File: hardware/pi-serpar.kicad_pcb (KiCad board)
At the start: 2 copper layers, 65 x 56 mm, 31 parts, among them J2 40HAT, J3 IEEE1284, J4 IEEE1284, J5 RS232, J7 RS232, U1 CAT24C32, U2 SN74LVC161284DLR, U3 MAX3232

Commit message: v1 ordered at jlcpcb
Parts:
- JP1: footprint Jumper:SolderJumper-2_P1.3mm_Open_RoundedPad1.0x1.5mm -> Jumper:SolderJumper-2_P1.3mm_Bridged_Pad1.0x1.5mm
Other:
- board text added: "2"
- board text added: "3"
- board text added: "7"
- board text added: "8"
- board text added: "DB9 Pins"
- board text added: "RS232 setup"
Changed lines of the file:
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@@
       ))
   )
-  (footprint "Jumper:SolderJumper-2_P1.3mm_Open_RoundedPad1.0x1.5mm" (layer "B.Cu")
+  (footprint "Jumper:SolderJumper-2_P1.3mm_Bridged_Pad1.0x1.5mm" (layer "B.Cu")
     (at 135.748 71.882)
-    (descr "SMD Solder Jumper, 1x1.5mm, rounded Pads, 0.3mm gap, open")
-    (tags "solder jumper open")
+    (descr "SMD Solder Jumper, 1x1.5mm Pads, 0.3mm gap, bridged with 1 copper strip")
+    (tags "net tie solder jumper bridged")
     (property "Sheetfile" "pi-serpar.kicad_sch")
     (property "Sheetname" "")
-    (property "ki_description" "Solder Jumper, 2-pole, open")
+    (property "ki_description" "Solder Jumper, 2-pole, closed/bridged")
     (property "ki_keywords" "solder jumper SPST")
     (attr exclude_from_pos_files)
-    (fp_text reference "JP1" (at 0 1.8) (layer "B.SilkS") hide
+    (net_tie_pad_groups "1, 2")
+    (fp_text reference "JP1" (at 0 1.8 180) (layer "B.SilkS")
         (effects (font (size 1 1) (thickness 0.15)) (justify mirror))
     )
-    (fp_text value "EEPROM WP" (at 0 -1.9) (layer "B.SilkS")
+    (fp_text value "EEPROM WP" (at 0 -1.9 180) (layer "B.Fab")
         (effects (font (size 1 1) (thickness 0.15)) (justify mirror))
     )
-    (fp_line (start -1.4 -0.3) (end -1.4 0.3)
-      (stroke (width 0.12) (type solid)) (layer "B.SilkS"))
-    (fp_line (start -0.7 1) (end 0.7 1)
-      (stroke (width 0.12) (type solid)) (layer "B.SilkS"))
-    (fp_line (start 0.7 -1) (end -0.7 -1)
-      (stroke (width 0.12) (type solid)) (layer "B.SilkS"))
-    (fp_line (start 1.4 0.3) (end 1.4 -0.3)
-      (stroke (width 0.12) (type solid)) (layer "B.SilkS"))
-    (fp_arc (start -1.4 -0.3) (mid -1.194975 -0.794975) (end -0.7 -1)
-      (stroke (width 0.12) (type solid)) (layer "B.SilkS"))
-    (fp_arc (start -0.7 1) (mid -1.194975 0.794975) (end -1.4 0.3)
-      (stroke (width 0.12) (type solid)) (layer "B.SilkS"))
-    (fp_arc (start 0.7 -1) (mid 1.194975 -0.794975) (end 1.4 -0.3)
-      (stroke (width 0.12) (type solid)) (layer "B.SilkS"))
-    (fp_arc (start 1.4 0.3) (mid 1.194975 0.794975) (end 0.7 1)
+    (fp_poly
+      (pts
+        (xy -0.25 0.3)
+        (xy 0.25 0.3)
+        (xy 0.25 -0.3)
+        (xy -0.25 -0.3)
+      )
+      (stroke (width 0) (type solid)) (fill solid) (layer "B.Cu"))
+    (fp_line (start -1.4 -1) (end -1.4 1)
+      (stroke (width 0.12) (type solid)) (layer "B.SilkS"))
+    (fp_line (start -1.4 1) (end 1.4 1)
+      (stroke (width 0.12) (type solid)) (layer "B.SilkS"))
+    (fp_line (start 1.4 -1) (end -1.4 -1)
+      (stroke (width 0.12) (type solid)) (layer "B.SilkS"))
+    (fp_line (start 1.4 1) (end 1.4 -1)
       (stroke (width 0.12) (type solid)) (layer "B.SilkS"))
     (fp_line (start -1.65 1.25) (end -1.65 -1.25)
@@
     (fp_line (start 1.65 -1.25) (end 1.65 1.25)
       (stroke (width 0.05) (type solid)) (layer "B.CrtYd"))
-    (pad "1" smd custom (at -0.65 0) (size 1 0.5) (layers "B.Cu" "B.Mask")
-      (net 1 "GND") (pinfunction "A") (pintype "passive") (zone_connect 2) (thermal_bridge_angle 45)
-      (options (clearance outline) (anchor rect))
-      (primitives
-        (gr_circle (center 0 -0.25) (end 0.5 -0.25) (width 0) (fill yes))
-        (gr_circle (center 0 0.25) (end 0.5 0.25) (width 0) (fill yes))
-        (gr_poly
-          (pts
-            (xy 0.5 -0.75)
-            (xy 0 -0.75)
-            (xy 0 0.75)
-            (xy 0.5 0.75)
-          )
-          (width 0) (fill yes))
-      ))
-    (pad "2" smd custom (at 0.65 0) (size 1 0.5) (layers "B.Cu" "B.Mask")
-      (net 54 "Net-(JP1-B)") (pinfunction "B") (pintype "passive") (zone_connect 2) (thermal_bridge_angle 45)
-      (options (clearance outline) (anchor rect))
-      (primitives
-        (gr_circle (center 0 -0.25) (end 0.5 -0.25) (width 0) (fill yes))
-        (gr_circle (center 0 0.25) (end 0.5 0.25) (width 0) (fill yes))
-        (gr_poly
-          (pts
-            (xy 0 -0.75)
-            (xy -0.5 -0.75)
-            (xy -0.5 0.75)
-            (xy 0 0.75)
-          )
-          (width 0) (fill yes))
-      ))
+    (pad "1" smd rect (at -0.65 0) (size 1 1.5) (layers "B.Cu" "B.Mask")
+      (net 1 "GND") (pinfunction "A") (pintype "passive"))
+    (pad "2" smd rect (at 0.65 0) (size 1 1.5) (layers "B.Cu" "B.Mask")
+      (net 54 "Net-(JP1-B)") (pinfunction "B") (pintype "passive"))
   )
   (gr_poly
@@
   (gr_line (start 78.546356 63.817611) (end 78.546356 113.817611)
     (stroke (width 0.1) (type solid)) (layer "Edge.Cuts"))
+  (gr_text "RS232 setup" (at 124.714 82.804) (layer "B.SilkS")
+    (effects (font (size 1 1) (thickness 0.15)) (justify right bottom mirror))
+  )
+  (gr_text "7" (at 104.902 80.264) (layer "B.SilkS")
+    (effects (font (size 1 1) (thickness 0.15)) (justify right bottom mirror))
+  )
+  (gr_text "2" (at 102.362 80.264) (layer "B.SilkS")
+    (effects (font (size 1 1) (thickness 0.15)) (justify right bottom mirror))
+  )
   (gr_text "Null-Modem DB9F" (at 109.45 81.788) (layer "B.SilkS")
-    (effects (font (size 1 1) (thickness 0.2) bold) (justify right bottom mirror))
+    (effects (font (size 1 1) (thickness 0.15)) (justify right bottom mirror))
   )
   (gr_text "pi-serpar v1\nhttps://github.com/hanshuebner/pi-serpar" (at 137.14 102.36) (layer "B.SilkS")
     (effects (font (size 1.5 1.5) (thickness 0.18)) (justify left bottom mirror))
   )
+  (gr_text "DB9 Pins" (at 100.838 78.74) (layer "B.SilkS")
+    (effects (font (size 1 1) (thickness 0.15)) (justify right bottom mirror))
+  )
+  (gr_text "3" (at 99.822 80.264) (layer "B.SilkS")
+    (effects (font (size 1 1) (thickness 0.15)) (justify right bottom mirror))
+  )
+  (gr_text "8" (at 107.442 80.264) (layer "B.SilkS")
+    (effects (font (size 1 1) (thickness 0.15)) (justify right bottom mirror))
+  )
   (gr_text "1:1 DB9M" (at 109.22 84.582) (layer "B.SilkS")
-    (effects (font (size 1 1) (thickness 0.2) bold) (justify right bottom mirror))
+    (effects (font (size 1 1) (thickness 0.15)) (justify right bottom mirror))
   )
   (gr_text "pi-serpar v1" (at 136.77 80.64) (layer "F.SilkS")

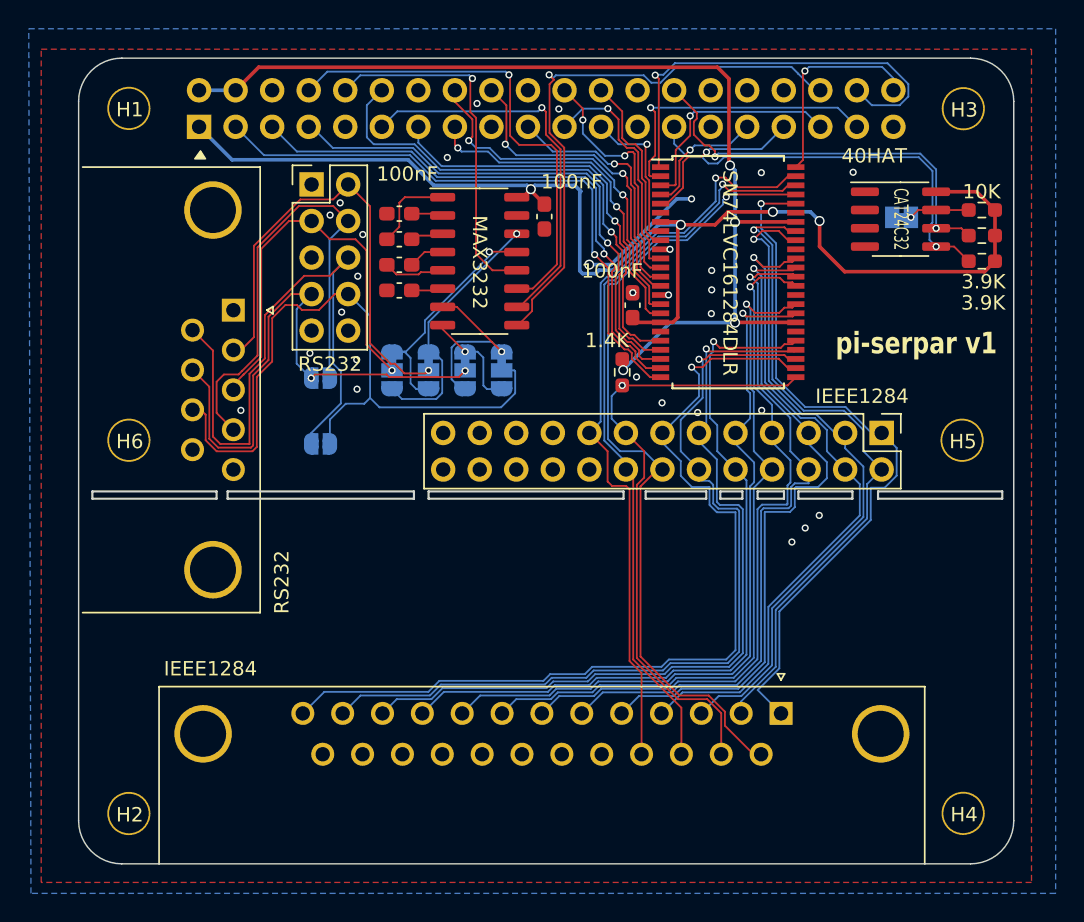
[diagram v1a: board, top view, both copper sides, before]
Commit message: IEEE1284 in TSSOP-48 package
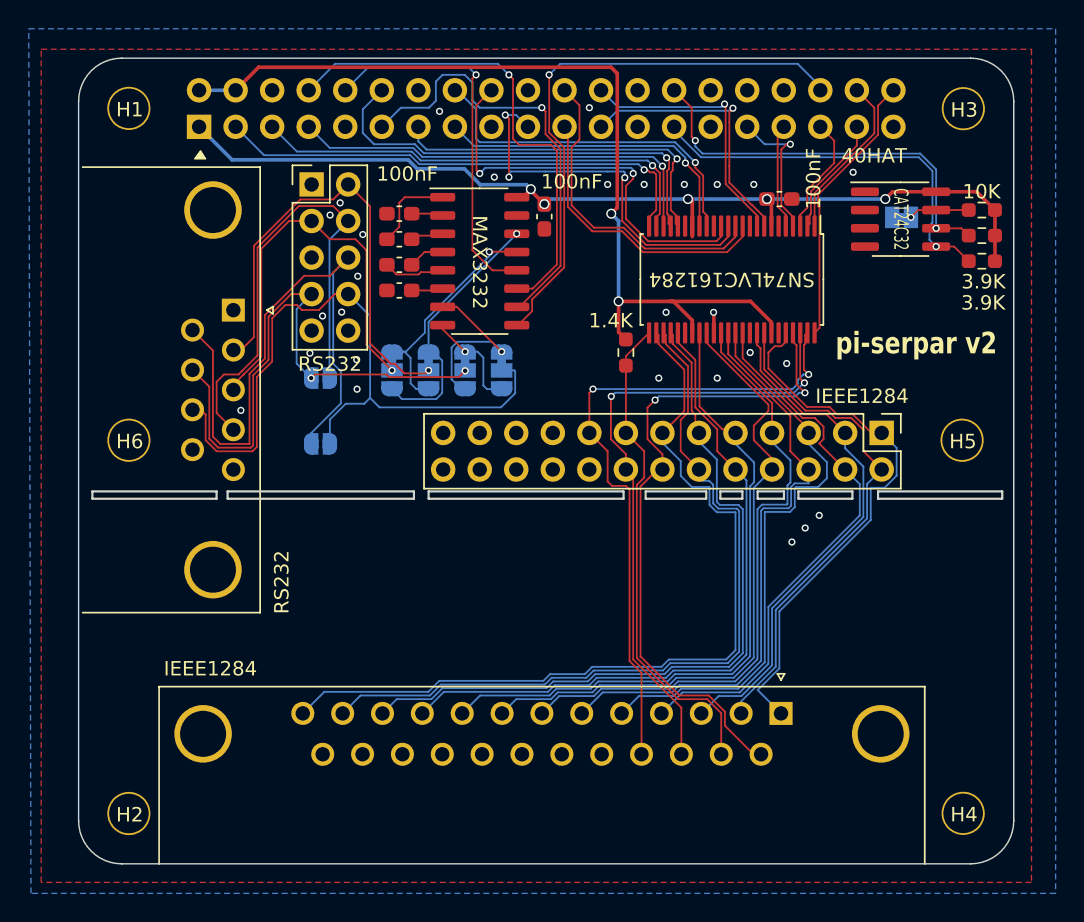
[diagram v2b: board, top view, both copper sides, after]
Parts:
- U2: value SN74LVC161284DLR -> SN74LVC161284; footprint Package_SO:SSOP-48_7.5x15.9mm_P0.635mm -> Package_SO:TSSOP-48_6.1x12.5mm_P0.5mm
- moved C2 12.6 mm to (127.3, 70.6), turned to 0 degrees
- moved R5 1.40 mm to (116.6, 81.3)
- moved U2 0.57 mm to (124.0, 76.2), turned to -90 degrees
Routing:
- net +3V3: track 89.9 -> 67.5 mm, vias 4 -> 5
- net /GPIO20: track 30.0 -> 11.7 mm, vias 1 -> 0
- net /GPIO26: track 20.7 -> 8.32 mm, vias 1 -> 0
- net /CONTROL1: track 56.8 -> 45.3 mm, vias 1 -> 2
- net /CONTROL0: track 49.0 -> 38.2 mm, vias 1 -> 0
- net /DATA0: track 46.2 -> 35.4 mm, vias 1 -> 0
- net /DATA1: track 46.5 -> 36.0 mm, vias 1 -> 0
- net /GPIO10: track 17.2 -> 26.7 mm, vias 1 -> 3
- net +5V: track 73.4 -> 63.9 mm, vias 4 -> 2
- net /STATUS3: track 43.0 -> 34.3 mm, vias 1 -> 0
- net /CONTROL2: track 52.0 -> 43.6 mm, vias 1 -> 2
- net /GPIO11: track 10.6 -> 19.0 mm
- net GND: track 9.65 -> 1.43 mm, vias 29 -> 28
- net /DATA2: track 46.8 -> 38.6 mm, vias 1 -> 0
- net /GPIO2: track 42.2 -> 34.4 mm
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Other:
- board text added: "pi-serpar v2"
- board text added: "pi-serpar v2 https://github.com/hanshuebner/pi-serpar"
- board text removed: "1:1 DB9M"
- board text removed: "pi-serpar v1"
- board text removed: "pi-serpar v1 https://github.com/hanshuebner/pi-serpar"

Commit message: fix idc footprints, add db9h
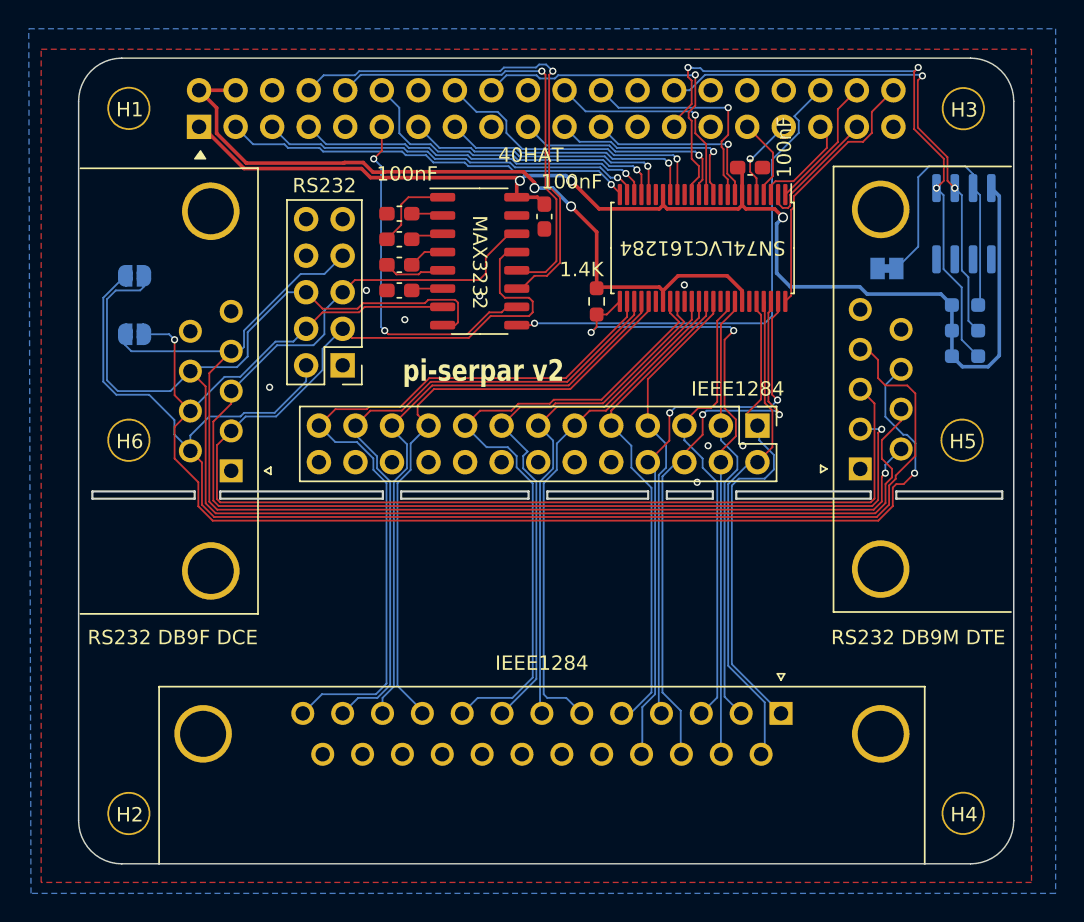
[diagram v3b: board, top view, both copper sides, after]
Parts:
- removed JP4: TX_SEL, Jumper:SolderJumper-3_P1.3mm_Bridged12_RoundedPad1.0x1.5mm
- removed JP5: RTS_SEL, Jumper:SolderJumper-3_P1.3mm_Bridged12_RoundedPad1.0x1.5mm
- removed JP6: RX_SEL, Jumper:SolderJumper-3_P1.3mm_Bridged12_RoundedPad1.0x1.5mm
- removed JP7: CTS_SEL, Jumper:SolderJumper-3_P1.3mm_Bridged12_RoundedPad1.0x1.5mm
- added J1: RS232 DB9M DTE, Connector_Dsub:DSUB-9_Male_Horizontal_P2.77x2.84mm_EdgePinOffset7.70mm_Housed_MountingHolesOffset9.12mm, F.Cu at (132.9, 89.4)
- J5: value RS232 -> RS232 DB9F DCE; footprint Connector_Dsub:DSUB-9_Male_Horizontal_P2.77x2.84mm_EdgePinOffset7.70mm_Housed_MountingHolesOffset9.12mm -> Connector_Dsub:DSUB-9_Female_Horizontal_P2.77x2.84mm_EdgePinOffset7.70mm_Housed_MountingHolesOffset9.12mm
- R2, R3, R4, U1: moved to B.Cu
- moved JP3 17.4 mm to (82.4, 75.9)
- moved JP2 13.3 mm to (82.4, 80.0), turned to 0 degrees
- moved J7 12.8 mm to (96.9, 82.2), turned to 180 degrees
- moved J5 11.2 mm to (89.2, 89.5)
- moved J3 8.65 mm to (125.7, 86.4)
- moved R2 6.71 mm to (140.2, 78.0), turned to 180 degrees
- moved R3 6.71 mm to (140.2, 81.5), turned to 0 degrees
- moved R4 6.71 mm to (140.2, 79.8), turned to 0 degrees
- moved U1 4.42 mm to (140.1, 72.3), turned to 90 degrees
- moved R5 4.10 mm to (114.6, 77.7)
- moved JP1 3.70 mm to (134.7, 75.4)
- moved U2 2.99 mm to (121.9, 74.0)
- moved C2 2.99 mm to (125.2, 68.4)
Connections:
- U3 pad 13: RS232_RX -> RX
- U3 pad 14: RS232_TX -> TX
- U3 pad 7: RS232_RTS -> RTS
- U3 pad 8: RS232_CTS -> CTS
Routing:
- net RX: track 32.6 -> 91.8 mm, vias 1 -> 0
- net TX: track 28.3 -> 86.6 mm
- net CTS: track 48.1 -> 106.2 mm
- net RTS: track 39.4 -> 97.0 mm
- net DSR: track 42.0 -> 94.8 mm
- net DTR: track 33.8 -> 82.0 mm, vias 0 -> 1
- net +3V3: track 67.5 -> 87.4 mm, vias 5 -> 3
- net RS232_TX: track 17.8 -> 0.00 mm, vias 1 -> 0
- net RS232_RX: track 16.7 -> 0.00 mm, vias 1 -> 0
- net Net-(JP1-B): track 4.23 -> 20.5 mm, vias 1 -> 0
- net /ID_SD_EEPROM: track 27.6 -> 43.0 mm, vias 1 -> 3
- net RS232_RTS: track 12.5 -> 0.00 mm, vias 1 -> 0
- net +5V: track 63.9 -> 52.1 mm
- net /GPIO10: track 26.7 -> 15.6 mm, vias 3 -> 1
- net /CONTROL1: track 45.3 -> 34.5 mm, vias 2 -> 0
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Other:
- outline, holes or cut-outs redrawn
- board text removed: "2"
- board text removed: "3"
- board text removed: "7"
- board text removed: "8"
- board text removed: "DB9 Pins"
- board text removed: "Null-Modem DB9F"
- board text removed: "RS232 setup"

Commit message: v3 with dual db9 footprints
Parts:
- C1, C2, C3, C4, C5, C6: value 100nF -> 100n
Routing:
- net GND: vias 8 -> 10
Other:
- board text added: "pi-serpar v3"
- board text removed: "pi-serpar v2"
